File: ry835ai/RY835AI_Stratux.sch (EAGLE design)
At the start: 2 parts, among them X1 RASPI_BOARD_B+_HD

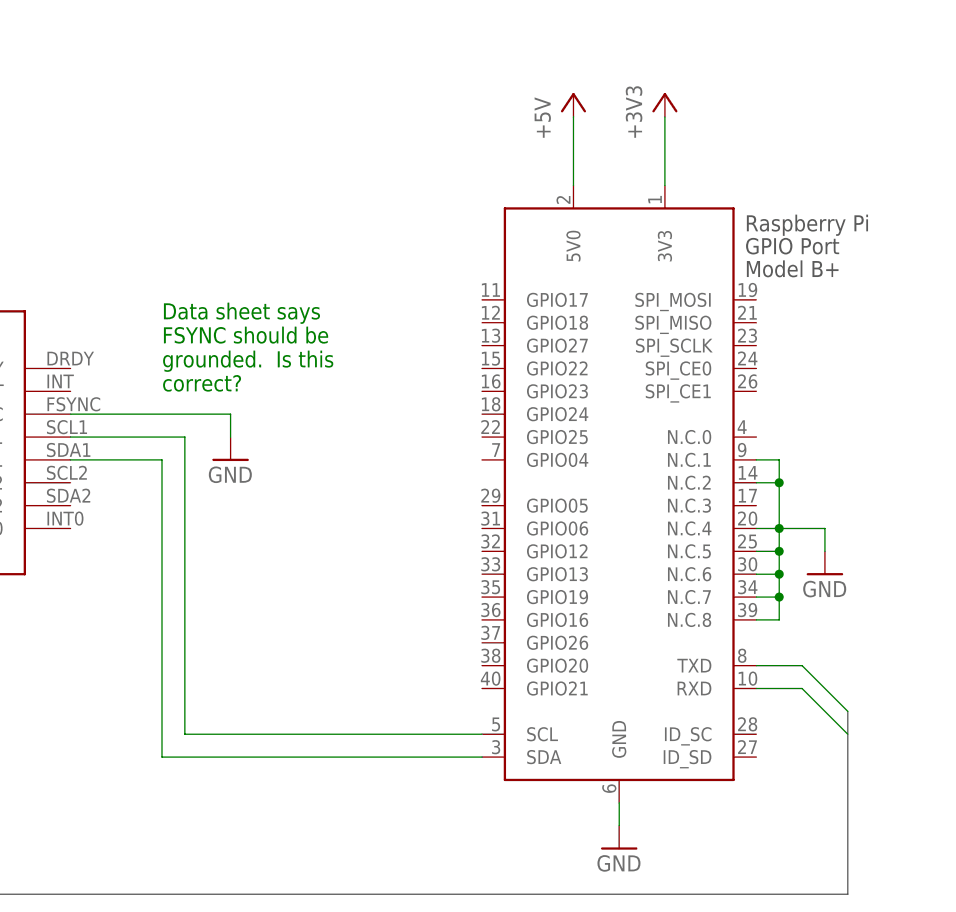
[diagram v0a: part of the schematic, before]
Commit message: Added bypass caps and cut-jumper for FSYNC signal. Added image to readme.md
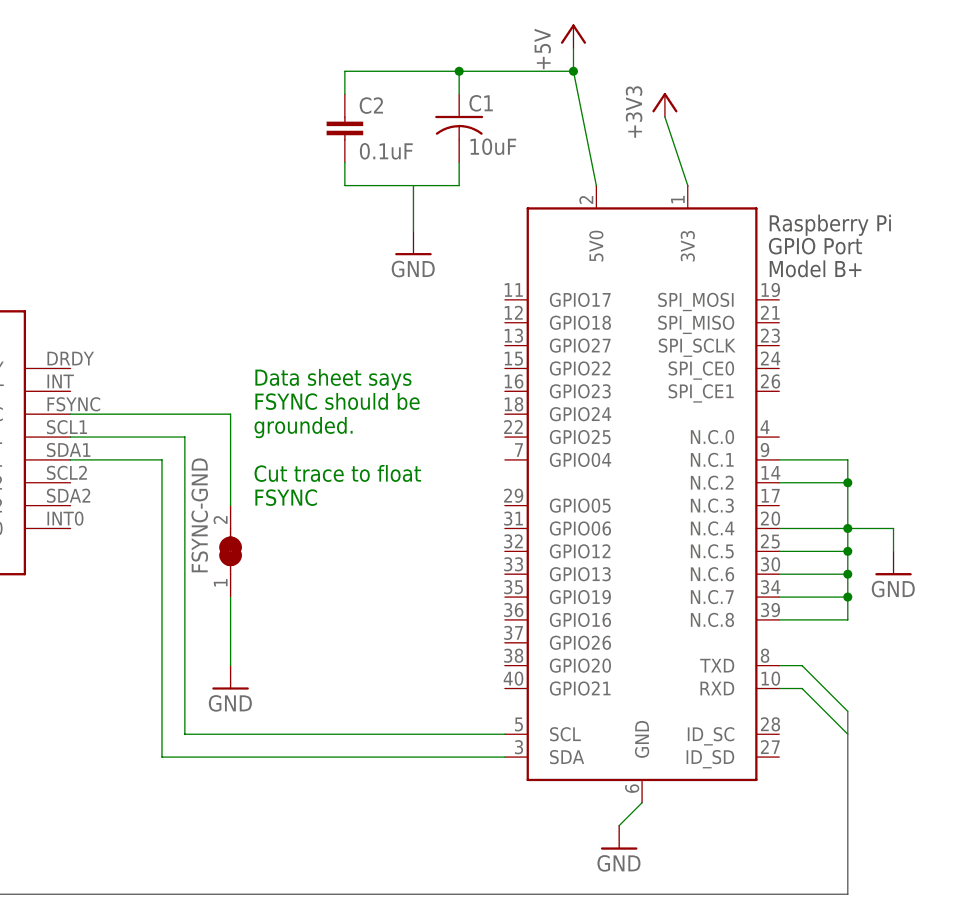
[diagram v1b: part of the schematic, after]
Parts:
- added C1: 10uF, rcl:C-USC0805
- added C2: 0.1uF, rcl:C-EUC0805
- added FSYNC-GND: (no value), jblib:CUTJUMPER
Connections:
- new net N$3: FSYNC-GND.2, U$1.FSYNC
- net +5V: now also C1.1, C2.1
- net GND: now also C1.2, C2.2, FSYNC-GND.1; no longer U$1.FSYNC
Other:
- note added: "Data sheet says FSYNC should be grounded. Cut trace to float FSYNC"
- note removed: "Data sheet says FSYNC should be grounded. Is this correct?"

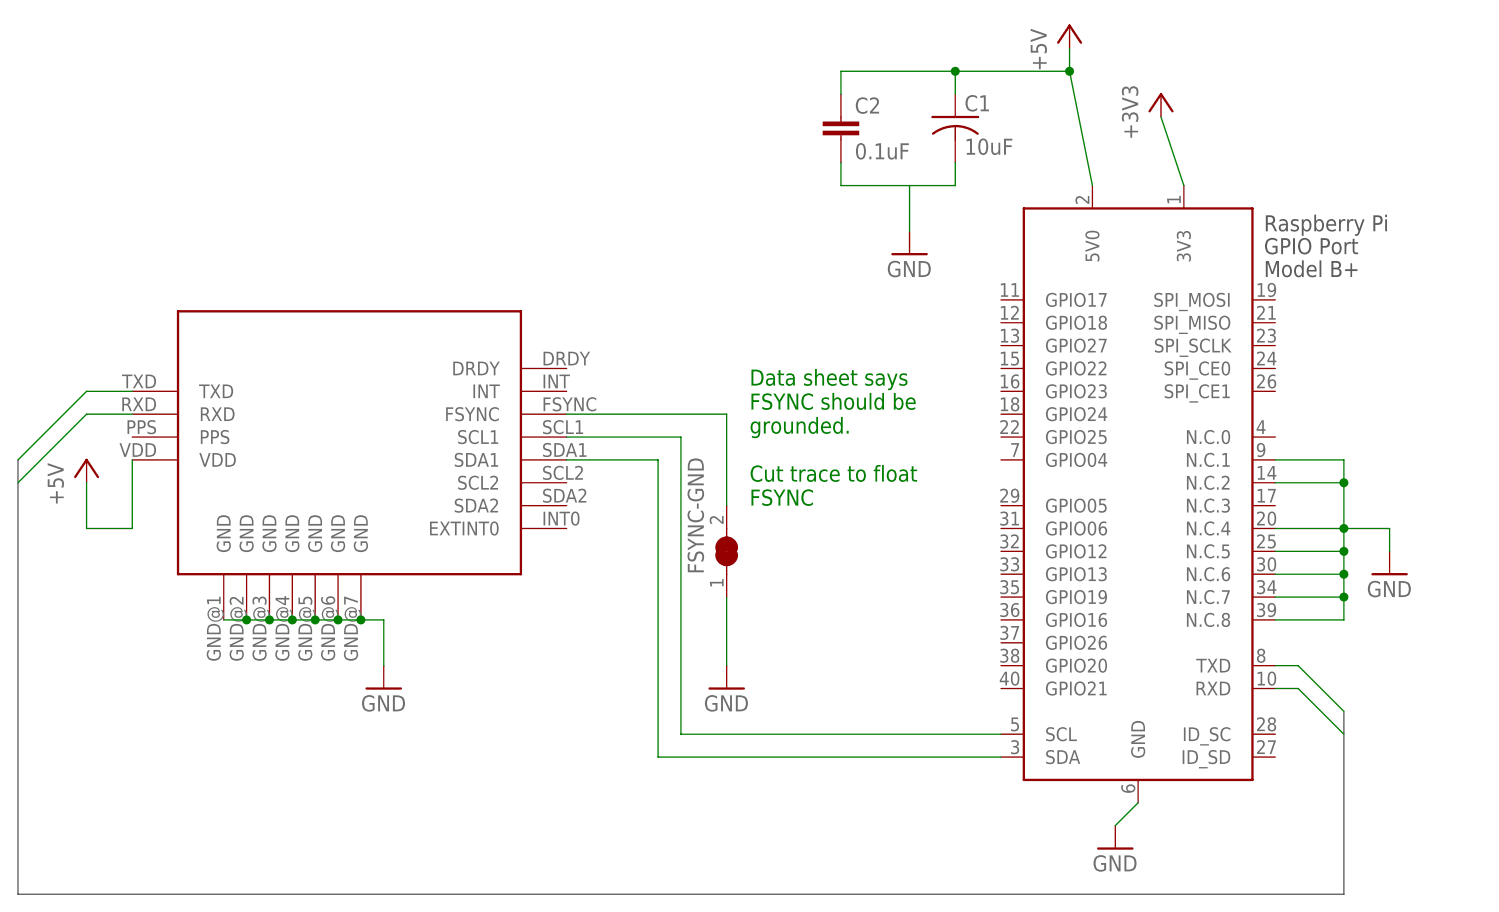
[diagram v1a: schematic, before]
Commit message: Keepout area added underneith GPS antenna area. Pads around mount points redeuced and made round to make room for signal traces.
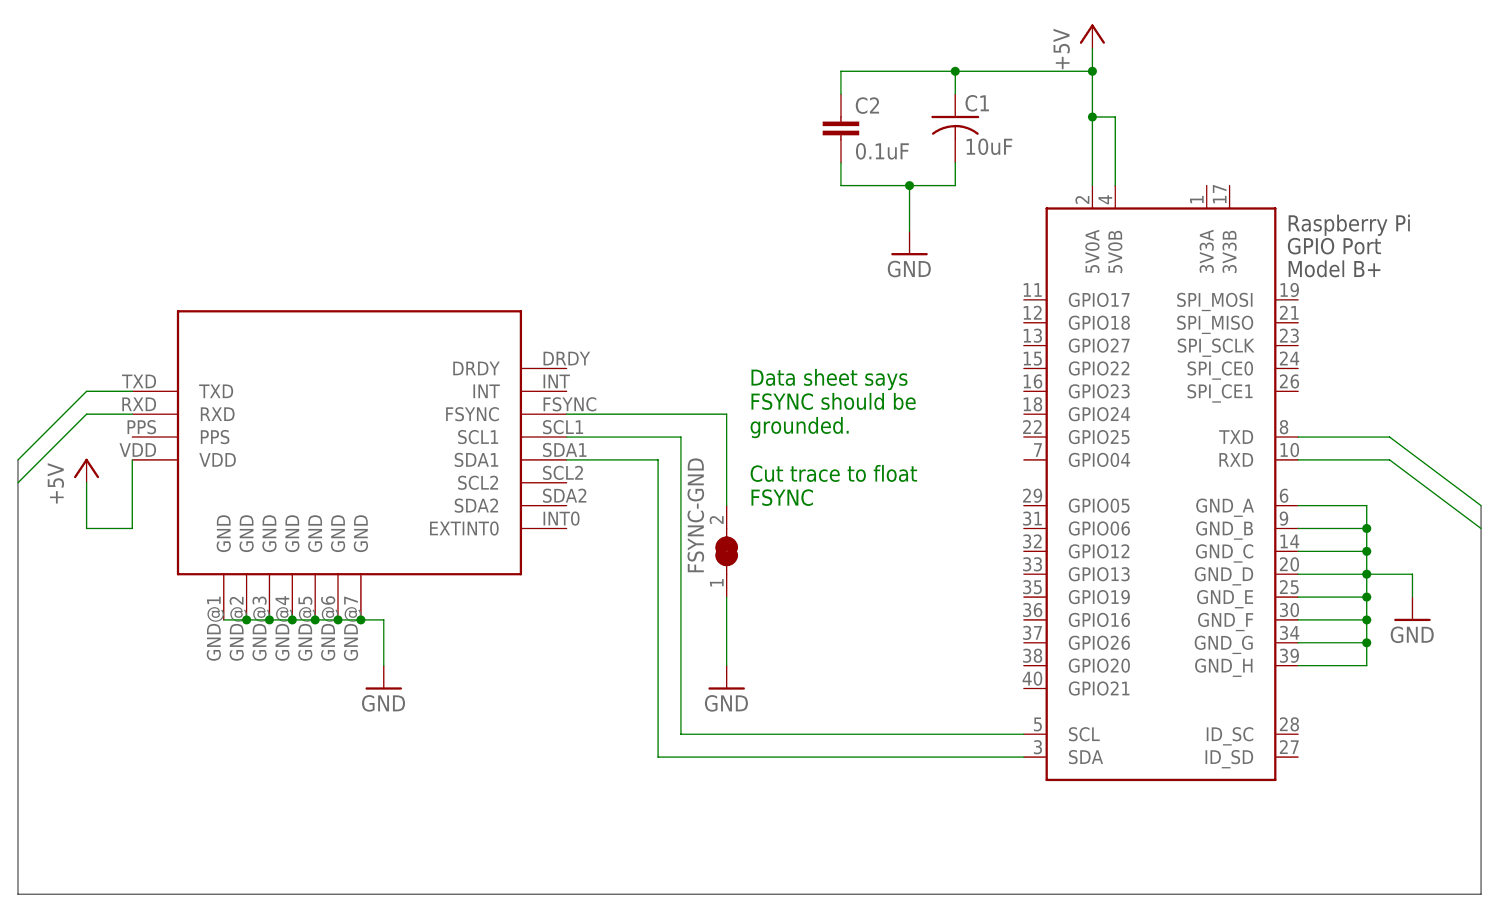
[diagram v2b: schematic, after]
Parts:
- removed X1: RASPI_BOARD_B+_HD, raspberrypi_bastelstube_v13:RASPI_BOARD_B+_HD
- added X2: RASPI_BOARD_B+#_HD, raspberrypi_bastelstube_v13:RASPI_BOARD_B+#_HD
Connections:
- removed net +3V3: X1.3V3
- net +5V: now also X2.5V0A, X2.5V0B; no longer X1.5V0
- net GND: now also X2.GND_A, X2.GND_B, X2.GND_C, X2.GND_D, X2.GND_E, X2.GND_F, X2.GND_G, X2.GND_H; no longer X1.GND, X1.N.C.1, X1.N.C.2, X1.N.C.4, X1.N.C.5, X1.N.C.6, X1.N.C.7, X1.N.C.8
- net N$1: now also X2.SDA; no longer X1.SDA
- net N$2: now also X2.SCL; no longer X1.SCL
- net RXTX_BUS0: now also X2.TXD; no longer X1.TXD
- net RXTX_BUS1: now also X2.RXD; no longer X1.RXD
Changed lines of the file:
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@@
 <parts>
 <part name="GND1" library="supply1" deviceset="GND" device=""/>
-<part name="GND2" library="supply1" deviceset="GND" device=""/>
 <part name="P+1" library="supply1" deviceset="+5V" device=""/>
 <part name="P+2" library="supply1" deviceset="+5V" device=""/>
 <part name="GND3" library="supply1" deviceset="GND" device=""/>
-<part name="X1" library="raspberrypi_bastelstube_v13" deviceset="RASPI_BOARD_B+" device="_HD"/>
 <part name="U$1" library="RY835AI" deviceset="RY835AI" device=""/>
-<part name="+3V1" library="supply1" deviceset="+3V3" device=""/>
 <part name="GND4" library="supply1" deviceset="GND" device=""/>
 <part name="C1" library="rcl" deviceset="C-US" device="C0805" value="10uF"/>
@@
 <part name="GND5" library="supply1" deviceset="GND" device=""/>
 <part name="FSYNC-GND" library="jblib" deviceset="CUTJUMPER" device=""/>
+<part name="X2" library="raspberrypi_bastelstube_v13" deviceset="RASPI_BOARD_B+#" device="_HD"/>
 </parts>
 <sheets>
@@
 <instances>
 <instance part="GND1" gate="1" x="58.42" y="17.78"/>
-<instance part="GND2" gate="1" x="139.7" y="0"/>
-<instance part="P+1" gate="1" x="134.62" y="91.44"/>
+<instance part="P+1" gate="1" x="137.16" y="91.44"/>
 <instance part="P+2" gate="1" x="25.4" y="43.18"/>
 <instance part="GND3" gate="1" x="96.52" y="17.78"/>
-<instance part="X1" gate="G$1" x="142.24" y="45.72"/>
 <instance part="U$1" gate="G$1" x="55.88" y="45.72"/>
-<instance part="+3V1" gate="G$1" x="144.78" y="83.82"/>
-<instance part="GND4" gate="1" x="170.18" y="30.48"/>
+<instance part="GND4" gate="1" x="172.72" y="25.4"/>
 <instance part="C1" gate="G$1" x="121.92" y="81.28"/>
 <instance part="C2" gate="G$1" x="109.22" y="81.28"/>
 <instance part="GND5" gate="1" x="116.84" y="66.04"/>
 <instance part="FSYNC-GND" gate="1" x="96.52" y="33.02" rot="R90"/>
+<instance part="X2" gate="G$1" x="144.78" y="45.72"/>
 </instances>
 <busses>
 <bus name="RXTX_BUS[0..1]">
 <segment>
-<wire x1="165.1" y1="15.24" x2="165.1" y2="-5.08" width="0.762" layer="92"/>
-<wire x1="165.1" y1="-5.08" x2="17.78" y2="-5.08" width="0.762" layer="92"/>
+<wire x1="180.34" y1="38.1" x2="180.34" y2="-5.08" width="0.762" layer="92"/>
+<wire x1="180.34" y1="-5.08" x2="17.78" y2="-5.08" width="0.762" layer="92"/>
 <wire x1="17.78" y1="-5.08" x2="17.78" y2="43.18" width="0.762" layer="92"/>
 </segment>
@@
 </segment>
 <segment>
-<pinref part="GND2" gate="1" pin="GND"/>
-<wire x1="139.7" y1="2.54" x2="142.24" y2="5.08" width="0.1524" layer="91"/>
-<pinref part="X1" gate="G$1" pin="GND"/>
-</segment>
-<segment>
-<pinref part="X1" gate="G$1" pin="N.C.1"/>
-<wire x1="157.48" y1="43.18" x2="165.1" y2="43.18" width="0.1524" layer="91"/>
-<wire x1="165.1" y1="43.18" x2="165.1" y2="40.64" width="0.1524" layer="91"/>
-<pinref part="X1" gate="G$1" pin="N.C.2"/>
-<wire x1="165.1" y1="40.64" x2="157.48" y2="40.64" width="0.1524" layer="91"/>
-<wire x1="165.1" y1="40.64" x2="165.1" y2="35.56" width="0.1524" layer="91"/>
-<pinref part="X1" gate="G$1" pin="N.C.4"/>
-<wire x1="165.1" y1="35.56" x2="157.48" y2="35.56" width="0.1524" layer="91"/>
-<wire x1="165.1" y1="35.56" x2="165.1" y2="33.02" width="0.1524" layer="91"/>
-<pinref part="X1" gate="G$1" pin="N.C.5"/>
-<wire x1="165.1" y1="33.02" x2="157.48" y2="33.02" width="0.1524" layer="91"/>
-<wire x1="165.1" y1="33.02" x2="165.1" y2="30.48" width="0.1524" layer="91"/>
-<pinref part="X1" gate="G$1" pin="N.C.6"/>
-<wire x1="165.1" y1="30.48" x2="157.48" y2="30.48" width="0.1524" layer="91"/>
-<wire x1="165.1" y1="30.48" x2="165.1" y2="27.94" width="0.1524" layer="91"/>
-<pinref part="X1" gate="G$1" pin="N.C.7"/>
-<wire x1="165.1" y1="27.94" x2="157.48" y2="27.94" width="0.1524" layer="91"/>
-<wire x1="165.1" y1="27.94" x2="165.1" y2="25.4" width="0.1524" layer="91"/>
-<pinref part="X1" gate="G$1" pin="N.C.8"/>
-<wire x1="165.1" y1="25.4" x2="157.48" y2="25.4" width="0.1524" layer="91"/>
-<junction x="165.1" y="40.64"/>
-<junction x="165.1" y="35.56"/>
-<junction x="165.1" y="33.02"/>
-<junction x="165.1" y="30.48"/>
-<junction x="165.1" y="27.94"/>
-<wire x1="165.1" y1="35.56" x2="170.18" y2="35.56" width="0.1524" layer="91"/>
-<wire x1="170.18" y1="35.56" x2="170.18" y2="33.02" width="0.1524" layer="91"/>
+<wire x1="160.02" y1="38.1" x2="167.64" y2="38.1" width="0.1524" layer="91"/>
+<wire x1="167.64" y1="38.1" x2="167.64" y2="35.56" width="0.1524" layer="91"/>
+<wire x1="167.64" y1="35.56" x2="160.02" y2="35.56" width="0.1524" layer="91"/>
+<wire x1="167.64" y1="35.56" x2="167.64" y2="33.02" width="0.1524" layer="91"/>
+<wire x1="167.64" y1="33.02" x2="167.64" y2="30.48" width="0.1524" layer="91"/>
+<wire x1="167.64" y1="30.48" x2="160.02" y2="30.48" width="0.1524" layer="91"/>
+<wire x1="167.64" y1="30.48" x2="167.64" y2="27.94" width="0.1524" layer="91"/>
+<wire x1="167.64" y1="27.94" x2="160.02" y2="27.94" width="0.1524" layer="91"/>
+<wire x1="167.64" y1="27.94" x2="167.64" y2="25.4" width="0.1524" layer="91"/>
+<wire x1="167.64" y1="25.4" x2="160.02" y2="25.4" width="0.1524" layer="91"/>
+<wire x1="167.64" y1="25.4" x2="167.64" y2="22.86" width="0.1524" layer="91"/>
+<wire x1="167.64" y1="22.86" x2="160.02" y2="22.86" width="0.1524" layer="91"/>
+<wire x1="167.64" y1="22.86" x2="167.64" y2="20.32" width="0.1524" layer="91"/>
+<wire x1="167.64" y1="20.32" x2="160.02" y2="20.32" width="0.1524" layer="91"/>
+<junction x="167.64" y="35.56"/>
+<junction x="167.64" y="30.48"/>
+<junction x="167.64" y="27.94"/>
+<junction x="167.64" y="25.4"/>
+<junction x="167.64" y="22.86"/>
+<wire x1="167.64" y1="30.48" x2="172.72" y2="30.48" width="0.1524" layer="91"/>
+<wire x1="172.72" y1="30.48" x2="172.72" y2="27.94" width="0.1524" layer="91"/>
 <pinref part="GND4" gate="1" pin="GND"/>
+<pinref part="X2" gate="G$1" pin="GND_C"/>
+<wire x1="160.02" y1="33.02" x2="167.64" y2="33.02" width="0.1524" layer="91"/>
+<junction x="167.64" y="33.02"/>
+<pinref part="X2" gate="G$1" pin="GND_A"/>
+<pinref part="X2" gate="G$1" pin="GND_B"/>
+<pinref part="X2" gate="G$1" pin="GND_D"/>
+<pinref part="X2" gate="G$1" pin="GND_E"/>
+<pinref part="X2" gate="G$1" pin="GND_F"/>
+<pinref part="X2" gate="G$1" pin="GND_G"/>
+<pinref part="X2" gate="G$1" pin="GND_H"/>
 </segment>
 <segment>
@@
 <wire x1="116.84" y1="73.66" x2="116.84" y2="68.58" width="0.1524" layer="91"/>
 <pinref part="GND5" gate="1" pin="GND"/>
+<junction x="116.84" y="73.66"/>
 </segment>
 <segment>
@@
 <segment>
 <pinref part="P+1" gate="1" pin="+5V"/>
-<wire x1="134.62" y1="88.9" x2="134.62" y2="86.36" width="0.1524" layer="91"/>
-<pinref part="X1" gate="G$1" pin="5V0"/>
+<wire x1="137.16" y1="88.9" x2="137.16" y2="86.36" width="0.1524" layer="91"/>
 <pinref part="C2" gate="G$1" pin="1"/>
-<wire x1="134.62" y1="86.36" x2="137.16" y2="73.66" width="0.1524" layer="91"/>
+<wire x1="137.16" y1="86.36" x2="137.16" y2="81.28" width="0.1524" layer="91"/>
+<wire x1="137.16" y1="81.28" x2="137.16" y2="73.66" width="0.1524" layer="91"/>
 <wire x1="109.22" y1="83.82" x2="109.22" y2="86.36" width="0.1524" layer="91"/>
 <wire x1="109.22" y1="86.36" x2="121.92" y2="86.36" width="0.1524" layer="91"/>
 <pinref part="C1" gate="G$1" pin="1"/>
-<wire x1="121.92" y1="86.36" x2="134.62" y2="86.36" width="0.1524" layer="91"/>
+<wire x1="121.92" y1="86.36" x2="137.16" y2="86.36" width="0.1524" layer="91"/>
 <wire x1="121.92" y1="83.82" x2="121.92" y2="86.36" width="0.1524" layer="91"/>
 <junction x="121.92" y="86.36"/>
-<junction x="134.62" y="86.36"/>
+<junction x="137.16" y="86.36"/>
+<pinref part="X2" gate="G$1" pin="5V0A"/>
+<pinref part="X2" gate="G$1" pin="5V0B"/>
+<wire x1="139.7" y1="73.66" x2="139.7" y2="81.28" width="0.1524" layer="91"/>
+<wire x1="139.7" y1="81.28" x2="137.16" y2="81.28" width="0.1524" layer="91"/>
+<junction x="137.16" y="81.28"/>
 </segment>
 </net>
@@
 <wire x1="78.74" y1="43.18" x2="88.9" y2="43.18" width="0.1524" layer="91"/>
 <wire x1="88.9" y1="43.18" x2="88.9" y2="10.16" width="0.1524" layer="91"/>
-<wire x1="88.9" y1="10.16" x2="127" y2="10.16" width="0.1524" layer="91"/>
-<pinref part="X1" gate="G$1" pin="SDA"/>
+<wire x1="88.9" y1="10.16" x2="129.54" y2="10.16" width="0.1524" layer="91"/>
 <pinref part="U$1" gate="G$1" pin="SDA1"/>
+<pinref part="X2" gate="G$1" pin="SDA"/>
 </segment>
 </net>
@@
 <wire x1="78.74" y1="45.72" x2="91.44" y2="45.72" width="0.1524" layer="91"/>
 <wire x1="91.44" y1="45.72" x2="91.44" y2="12.7" width="0.1524" layer="91"/>
-<wire x1="91.44" y1="12.7" x2="127" y2="12.7" width="0.1524" layer="91"/>
-<pinref part="X1" gate="G$1" pin="SCL"/>
+<wire x1="91.44" y1="12.7" x2="129.54" y2="12.7" width="0.1524" layer="91"/>
 <pinref part="U$1" gate="G$1" pin="SCL1"/>
-</segment>
-</net>
-<net name="+3V3" class="0">
-<segment>
-<pinref part="X1" gate="G$1" pin="3V3"/>
-<pinref part="+3V1" gate="G$1" pin="+3V3"/>
-<wire x1="144.78" y1="81.28" x2="147.32" y2="73.66" width="0.1524" layer="91"/>
+<pinref part="X2" gate="G$1" pin="SCL"/>
 </segment>
 </net>
 <net name="RXTX_BUS0" class="0">
 <segment>
-<pinref part="X1" gate="G$1" pin="TXD"/>
-<wire x1="165.1" y1="15.24" x2="160.02" y2="20.32" width="0.1524" layer="91"/>
-<wire x1="160.02" y1="20.32" x2="157.48" y2="20.32" width="0.1524" layer="91"/>
+<wire x1="180.34" y1="38.1" x2="170.18" y2="45.72" width="0.1524" layer="91"/>
+<wire x1="170.18" y1="45.72" x2="160.02" y2="45.72" width="0.1524" layer="91"/>
+<pinref part="X2" gate="G$1" pin="TXD"/>
 </segment>
 <segment>
@@
 <net name="RXTX_BUS1" class="0">
 <segment>
-<pinref part="X1" gate="G$1" pin="RXD"/>
-<wire x1="165.1" y1="12.7" x2="160.02" y2="17.78" width="0.1524" layer="91"/>
-<wire x1="160.02" y1="17.78" x2="157.48" y2="17.78" width="0.1524" layer="91"/>
+<wire x1="180.34" y1="35.56" x2="170.18" y2="43.18" width="0.1524" layer="91"/>
+<wire x1="170.18" y1="43.18" x2="160.02" y2="43.18" width="0.1524" layer="91"/>
+<pinref part="X2" gate="G$1" pin="RXD"/>
 </segment>
 <segment>
@@
 </sheet>
 </sheets>
+<errors>
+</errors>
 </schematic>
 </drawing>
